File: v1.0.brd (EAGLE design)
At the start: 160 x 100 mm, 44 parts, among them J1 DC-044-A, Q3 6pF@32.7680kHz, U1 MCP23017-E/SO, U10 74HC139N, U2 MCP79412-I/SN, U3 LOPY, U4 GROVE_DC&DC

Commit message: pycom
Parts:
- added X1, X2, X3, X4: JST-XH-05-PIN-ROUND-PAD, Rembrandt Electronics - JST XH Connectors v1-0 2:JST-XH-05-PACKAGE-ROUND-PAD
- added X5: JST-XH-06-PIN-ROUND-PAD, Rembrandt Electronics - JST XH Connectors v1-0 2:JST-XH-06-PACKAGE-ROUND-PAD
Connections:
- removed net LOPY_P0: U3.P$2
- removed net LOPY_P1: U3.P$3
- removed net LOPY_P10: U3.P$12
- removed net LOPY_P11: U3.P$13
- removed net LOPY_P12: U3.P$14
- removed net LOPY_P3: U3.P$5
- removed net LOPY_P4: U3.P$6
- removed net LOPY_P9: U3.P$11
- new net LOPY_CS: X5.6
- new net LOPY_MISO: U3.P$14, X5.4
- new net LOPY_MOSI: U3.P$13, X5.3
- new net LOPY_RX0: U3.P$2, X1.4
- new net LOPY_RX1: U3.P$6, X2.4
- new net LOPY_SCL/CLK: U3.P$12, X3.5, X5.5
- new net LOPY_SDA: U3.P$11, X3.4
- new net LOPY_TX0: U3.P$3, X1.5
- new net LOPY_TX1: U3.P$5, X2.5
- net +5V: now also X1.1, X2.1, X3.1, X5.1
- net GND: now also X1.3, X2.3, X3.3
- net LOPY_3V3: now also X1.2, X2.2, X3.2, X5.2
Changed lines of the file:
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@@
 <attribute name="MPN" value="CC0603KRX7R9BB104" x="-224.79" y="-213.36" size="1.778" layer="27" display="off"/>
 </element>
+<element name="X1" library="Rembrandt Electronics - JST XH Connectors v1-0 2" package="JST-XH-05-PACKAGE-ROUND-PAD" value="JST-XH-05-PIN-ROUND-PAD" x="-213.36" y="-226.06"/>
+<element name="X2" library="Rembrandt Electronics - JST XH Connectors v1-0 2" package="JST-XH-05-PACKAGE-ROUND-PAD" value="JST-XH-05-PIN-ROUND-PAD" x="-213.36" y="-241.3"/>
+<element name="X3" library="Rembrandt Electronics - JST XH Connectors v1-0 2" package="JST-XH-05-PACKAGE-ROUND-PAD" value="JST-XH-05-PIN-ROUND-PAD" x="-213.36" y="-256.54"/>
+<element name="X4" library="Rembrandt Electronics - JST XH Connectors v1-0 2" package="JST-XH-05-PACKAGE-ROUND-PAD" value="JST-XH-05-PIN-ROUND-PAD" x="-213.36" y="-271.78"/>
+<element name="X5" library="Rembrandt Electronics - JST XH Connectors v1-0 2" package="JST-XH-06-PACKAGE-ROUND-PAD" value="JST-XH-06-PIN-ROUND-PAD" x="-212.09" y="-287.02"/>
 </elements>
 <signals>
@@
 <contactref element="C1" pad="2"/>
 <contactref element="C3" pad="2"/>
+<contactref element="X1" pad="3"/>
+<contactref element="X2" pad="3"/>
+<contactref element="X3" pad="3"/>
 <wire x1="-164.719" y1="-102.87" x2="-160.02" y2="-90.678" width="0" layer="19" extent="1-1"/>
 <wire x1="-148.59" y1="-68.58" x2="-160.02" y2="-90.678" width="0" layer="19" extent="1-1"/>
@@
 <wire x1="-219.71" y1="-214.122" x2="-214.63" y2="-185.928" width="0" layer="19" extent="1-1"/>
 <wire x1="-224.79" y1="-214.122" x2="-219.71" y2="-214.122" width="0" layer="19" extent="1-1"/>
+<wire x1="-213.36" y1="-226.06" x2="-219.71" y2="-214.122" width="0" layer="19" extent="1-1"/>
+<wire x1="-213.36" y1="-241.3" x2="-213.36" y2="-226.06" width="0" layer="19" extent="1-1"/>
+<wire x1="-213.36" y1="-256.54" x2="-213.36" y2="-241.3" width="0" layer="19" extent="1-1"/>
 <wire x1="-114.3" y1="4.572" x2="-129.54" y2="-43.688" width="0" layer="19" extent="1-1"/>
 <wire x1="-86.8934" y1="57.5818" x2="-114.3" y2="4.572" width="0" layer="19" extent="1-1"/>
@@
 <contactref element="C13" pad="2"/>
 <contactref element="U3" pad="P$28"/>
+<contactref element="X1" pad="1"/>
+<contactref element="X2" pad="1"/>
+<contactref element="X3" pad="1"/>
+<contactref element="X5" pad="1"/>
+<wire x1="-218.44" y1="-256.54" x2="-218.44" y2="-287.02" width="0" layer="19" extent="1-1"/>
+<wire x1="-218.44" y1="-241.3" x2="-218.44" y2="-256.54" width="0" layer="19" extent="1-1"/>
+<wire x1="-218.44" y1="-226.06" x2="-218.44" y2="-241.3" width="0" layer="19" extent="1-1"/>
+<wire x1="-184.15" y1="-71.12" x2="-218.44" y2="-226.06" width="0" layer="19" extent="1-1"/>
+<wire x1="-140.97" y1="-50.8" x2="-184.15" y2="-71.12" width="0" layer="19" extent="1-1"/>
 <wire x1="-129.54" y1="-45.212" x2="-140.97" y2="-50.8" width="0" layer="19" extent="1-1"/>
 <wire x1="-129.54" y1="-32.512" x2="-129.54" y2="-45.212" width="0" layer="19" extent="1-1"/>
-<wire x1="-184.15" y1="-71.12" x2="-140.97" y2="-50.8" width="0" layer="19" extent="1-1"/>
 <wire x1="-91.9734" y1="57.5818" x2="-129.54" y2="-32.512" width="0" layer="19" extent="1-1"/>
 <wire x1="-89.4334" y1="57.5818" x2="-91.9734" y2="57.5818" width="0" layer="19" extent="1-1"/>
@@
 <signal name="LOPY_3V3">
 <contactref element="U3" pad="P$26"/>
+<contactref element="X1" pad="2"/>
+<contactref element="X2" pad="2"/>
+<contactref element="X3" pad="2"/>
+<contactref element="X5" pad="2"/>
+<wire x1="-215.9" y1="-256.54" x2="-215.9" y2="-287.02" width="0" layer="19" extent="1-1"/>
+<wire x1="-215.9" y1="-241.3" x2="-215.9" y2="-256.54" width="0" layer="19" extent="1-1"/>
+<wire x1="-215.9" y1="-226.06" x2="-215.9" y2="-241.3" width="0" layer="19" extent="1-1"/>
+<wire x1="-184.15" y1="-76.2" x2="-215.9" y2="-226.06" width="0" layer="19" extent="1-1"/>
 </signal>
 <signal name="LOPY_RST">
 <contactref element="U3" pad="P$1"/>
 </signal>
-<signal name="LOPY_P0">
+<signal name="LOPY_RX0">
 <contactref element="U3" pad="P$2"/>
-</signal>
-<signal name="LOPY_P1">
+<contactref element="X1" pad="4"/>
+<wire x1="-201.93" y1="-73.66" x2="-210.82" y2="-226.06" width="0" layer="19" extent="1-1"/>
+</signal>
+<signal name="LOPY_TX0">
 <contactref element="U3" pad="P$3"/>
+<contactref element="X1" pad="5"/>
+<wire x1="-201.93" y1="-76.2" x2="-208.28" y2="-226.06" width="0" layer="19" extent="1-1"/>
 </signal>
 <signal name="LOPY_P2">
 <contactref element="U3" pad="P$4"/>
 </signal>
-<signal name="LOPY_P3">
+<signal name="LOPY_TX1">
 <contactref element="U3" pad="P$5"/>
-</signal>
-<signal name="LOPY_P4">
-<contactref element="U3" pad="P$6"/>
+<contactref element="X2" pad="5"/>
+<wire x1="-201.93" y1="-81.28" x2="-208.28" y2="-241.3" width="0" layer="19" extent="1-1"/>
 </signal>
 <signal name="LOPY_P8">
 <contactref element="U3" pad="P$10"/>
 </signal>
-<signal name="LOPY_P9">
+<signal name="LOPY_SDA">
 <contactref element="U3" pad="P$11"/>
-</signal>
-<signal name="LOPY_P10">
+<contactref element="X3" pad="4"/>
+<wire x1="-201.93" y1="-96.52" x2="-210.82" y2="-256.54" width="0" layer="19" extent="1-1"/>
+</signal>
+<signal name="LOPY_SCL/CLK">
 <contactref element="U3" pad="P$12"/>
-</signal>
-<signal name="LOPY_P11">
+<contactref element="X3" pad="5"/>
+<contactref element="X5" pad="5"/>
+<wire x1="-208.28" y1="-256.54" x2="-208.28" y2="-287.02" width="0" layer="19" extent="1-1"/>
+<wire x1="-201.93" y1="-99.06" x2="-208.28" y2="-256.54" width="0" layer="19" extent="1-1"/>
+</signal>
+<signal name="LOPY_MOSI">
 <contactref element="U3" pad="P$13"/>
-</signal>
-<signal name="LOPY_P12">
+<contactref element="X5" pad="3"/>
+<wire x1="-201.93" y1="-101.6" x2="-213.36" y2="-287.02" width="0" layer="19" extent="1-1"/>
+</signal>
+<signal name="LOPY_MISO">
 <contactref element="U3" pad="P$14"/>
+<contactref element="X5" pad="4"/>
+<wire x1="-201.93" y1="-104.14" x2="-210.82" y2="-287.02" width="0" layer="19" extent="1-1"/>
 </signal>
 <signal name="LOPY_P13">
@@
 <wire x1="-203.0222" y1="-168.275" x2="-212.09" y2="-215.646" width="0" layer="19" extent="1-1"/>
 </signal>
+<signal name="LOPY_RX1">
+<contactref element="X2" pad="4"/>
+<contactref element="U3" pad="P$6"/>
+<wire x1="-201.93" y1="-83.82" x2="-210.82" y2="-241.3" width="0" layer="19" extent="1-1"/>
+</signal>
+<signal name="LOPY_CS">
+<contactref element="X5" pad="6"/>
+</signal>
 </signals>

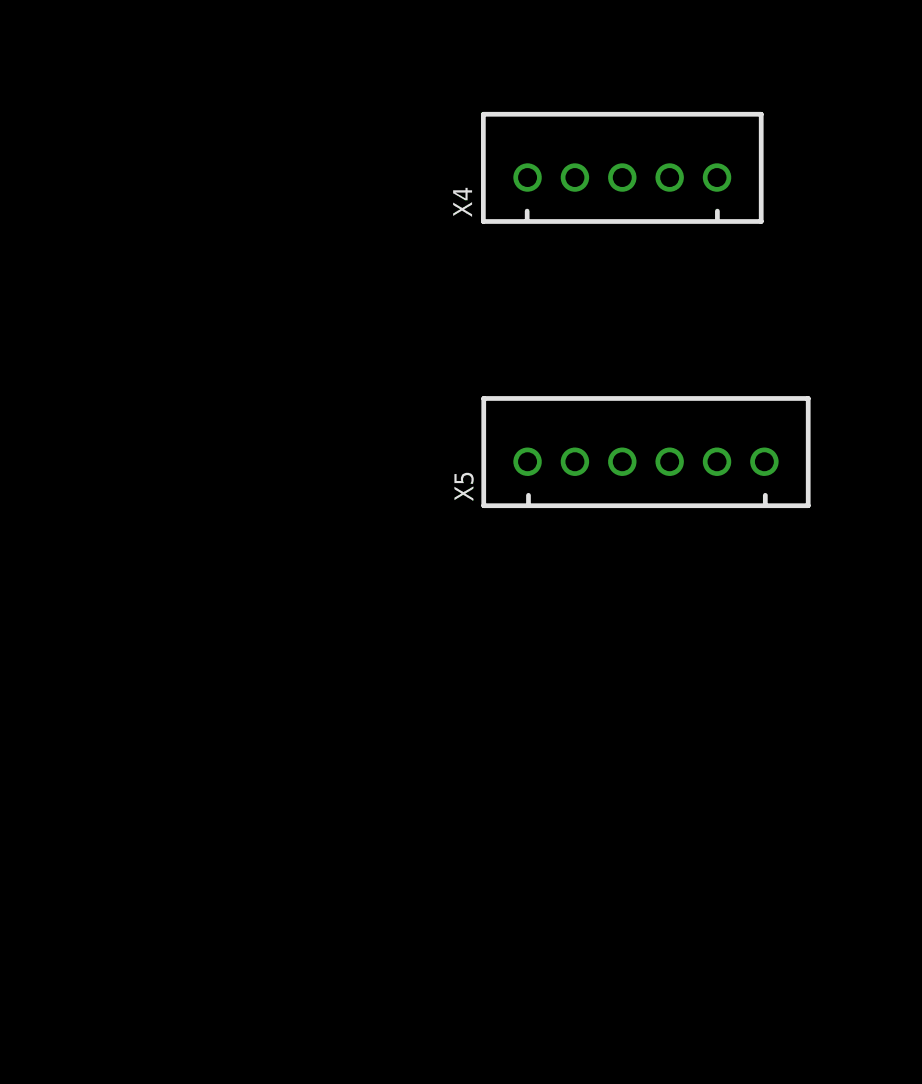
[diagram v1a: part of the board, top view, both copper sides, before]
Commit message: LDO for 5V
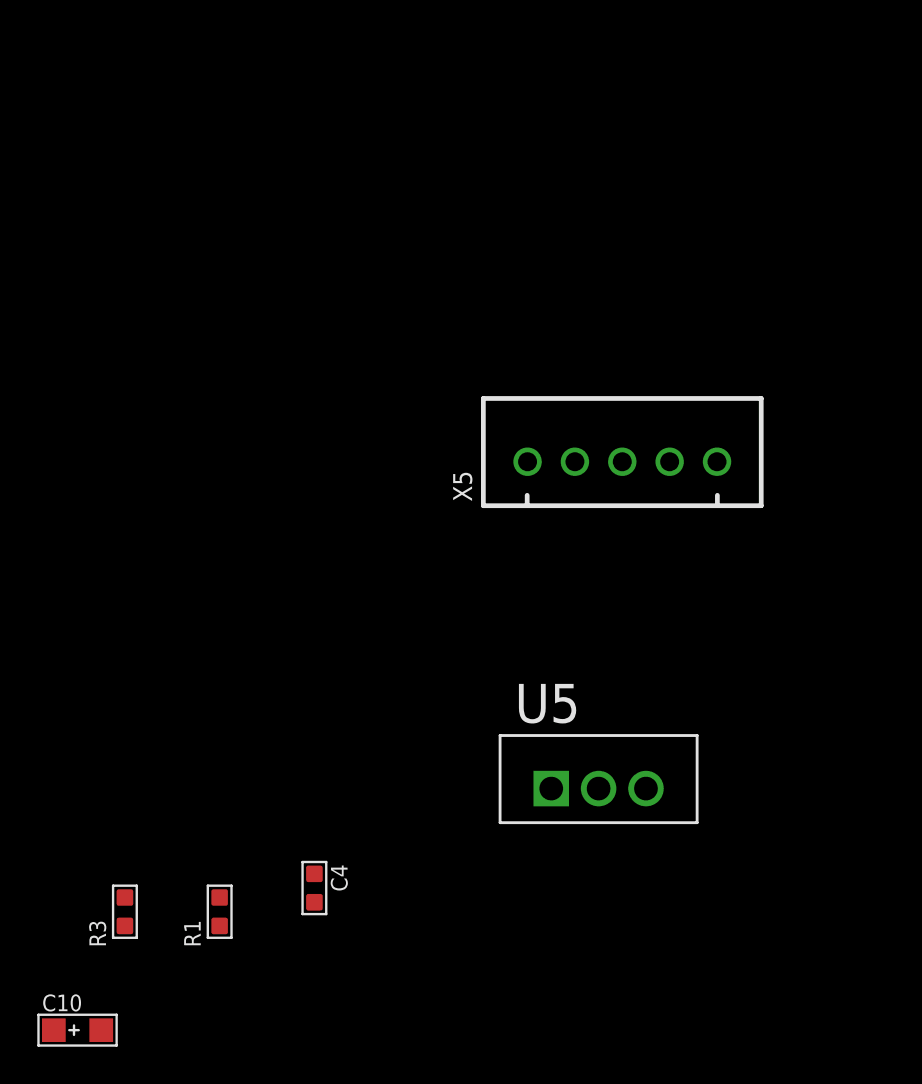
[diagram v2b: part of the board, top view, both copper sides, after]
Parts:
- removed X4: JST-XH-05-PIN-ROUND-PAD, Rembrandt Electronics - JST XH Connectors v1-0 2:JST-XH-05-PACKAGE-ROUND-PAD
- added C10: 10uf, Seeed-Capacitor:AVX-A
- added C4: 10uf, Seeed-Capacitor:C0603
- added R1: 3K, Seeed-Resistor:R0603
- added R3: 1K, Seeed-Resistor:R0603
- added U5: LM1085IT-5.0, imported-parts:TO254P470X1016X2222-3P
- X5: value JST-XH-06-PIN-ROUND-PAD -> JST-XH-05-PIN-ROUND-PAD; device Rembrandt Electronics - JST XH Connectors v1-0 2:JST-XH-06-PACKAGE-ROUND-PAD -> Rembrandt Electronics - JST XH Connectors v1-0 2:JST-XH-05-PACKAGE-ROUND-PAD
- moved X5 1.27 mm to (-213.4, -287.0)
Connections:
- removed net LOPY_CS: X5.6
- new net 6V5: C4.2, TP4.TP, U4.P$5, U4.P$6, U5.3
- new net N$5: R1.2, R3.1, U5.1
- net +5V: now also C10.-, R3.2, U5.2
- net 5V4: no longer TP4.TP, U4.P$5, U4.P$6
- net GND: now also C10.+, C4.1, R1.1
- net LOPY_MISO: now also X5.3; no longer X5.4
- net LOPY_MOSI: now also X5.4; no longer X5.3
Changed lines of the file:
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@@
 <element name="X2" library="Rembrandt Electronics - JST XH Connectors v1-0 2" package="JST-XH-05-PACKAGE-ROUND-PAD" value="JST-XH-05-PIN-ROUND-PAD" x="-213.36" y="-241.3"/>
 <element name="X3" library="Rembrandt Electronics - JST XH Connectors v1-0 2" package="JST-XH-05-PACKAGE-ROUND-PAD" value="JST-XH-05-PIN-ROUND-PAD" x="-213.36" y="-256.54"/>
-<element name="X4" library="Rembrandt Electronics - JST XH Connectors v1-0 2" package="JST-XH-05-PACKAGE-ROUND-PAD" value="JST-XH-05-PIN-ROUND-PAD" x="-213.36" y="-271.78"/>
-<element name="X5" library="Rembrandt Electronics - JST XH Connectors v1-0 2" package="JST-XH-06-PACKAGE-ROUND-PAD" value="JST-XH-06-PIN-ROUND-PAD" x="-212.09" y="-287.02"/>
+<element name="X5" library="Rembrandt Electronics - JST XH Connectors v1-0 2" package="JST-XH-05-PACKAGE-ROUND-PAD" value="JST-XH-05-PIN-ROUND-PAD" x="-213.36" y="-287.02"/>
+<element name="U5" library="imported-parts" package="TO254P470X1016X2222-3P" value="LM1085IT-5.0" x="-212.09" y="-303.53">
+<attribute name="MPN" value="LM1085IT-5.0" x="-212.09" y="-303.53" size="1.778" layer="27" display="off"/>
+<attribute name="OC_FARNELL" value="1469042" x="-212.09" y="-303.53" size="1.778" layer="27" display="off"/>
+<attribute name="OC_NEWARK" value="41K3382" x="-212.09" y="-303.53" size="1.778" layer="27" display="off"/>
+<attribute name="PACKAGE" value="TO-220" x="-212.09" y="-303.53" size="1.778" layer="27" display="off"/>
+<attribute name="SUPPLIER" value="National Semiconductor" x="-212.09" y="-303.53" size="1.778" layer="27" display="off"/>
+</element>
+<element name="C4" library="Seeed-Capacitor" library_urn="urn:adsk.eagle:library:464" package="C0603" value="10uf" x="-229.87" y="-309.88">
+<attribute name="MPN" value="CC0603KRX5R6BB106" x="-229.87" y="-309.88" size="1.778" layer="27" display="off"/>
+</element>
+<element name="R1" library="Seeed-Resistor" library_urn="urn:adsk.eagle:library:474" package="R0603" value="3K" x="-234.95" y="-311.15">
+<attribute name="MPN" value="RC0603FR-073KL" x="-234.95" y="-311.15" size="1.778" layer="27" display="off"/>
+</element>
+<element name="R3" library="Seeed-Resistor" library_urn="urn:adsk.eagle:library:474" package="R0603" value="1K" x="-240.03" y="-311.15">
+<attribute name="MPN" value="RC0603FR-071KL" x="-240.03" y="-311.15" size="1.778" layer="27" display="off"/>
+</element>
+<element name="C10" library="Seeed-Capacitor" library_urn="urn:adsk.eagle:library:464" package="AVX-A" value="10uf" x="-242.57" y="-317.5">
+<attribute name="MPN" value="TAJA106K010RNJ" x="-242.57" y="-317.5" size="1.778" layer="27" display="off"/>
+</element>
 </elements>
 <signals>
@@
 <contactref element="X2" pad="3"/>
 <contactref element="X3" pad="3"/>
+<contactref element="R1" pad="1"/>
+<contactref element="C4" pad="1"/>
+<contactref element="C10" pad="+"/>
 <wire x1="-164.719" y1="-102.87" x2="-160.02" y2="-90.678" width="0" layer="19" extent="1-1"/>
 <wire x1="-148.59" y1="-68.58" x2="-160.02" y2="-90.678" width="0" layer="19" extent="1-1"/>
@@
 <wire x1="-213.36" y1="-256.54" x2="-213.36" y2="-241.3" width="0" layer="19" extent="1-1"/>
 <wire x1="-114.3" y1="4.572" x2="-129.54" y2="-43.688" width="0" layer="19" extent="1-1"/>
+<wire x1="-229.87" y1="-309.118" x2="-213.36" y2="-256.54" width="0" layer="19" extent="1-1"/>
+<wire x1="-234.95" y1="-310.388" x2="-229.87" y2="-309.118" width="0" layer="19" extent="1-1"/>
+<wire x1="-243.84" y1="-317.5" x2="-234.95" y2="-310.388" width="0" layer="19" extent="1-1"/>
 <wire x1="-86.8934" y1="57.5818" x2="-114.3" y2="4.572" width="0" layer="19" extent="1-1"/>
 <wire x1="-81.8134" y1="55.0418" x2="-86.8934" y2="57.5818" width="0" layer="19" extent="1-1"/>
@@
 <contactref element="X3" pad="1"/>
 <contactref element="X5" pad="1"/>
+<contactref element="U5" pad="2"/>
+<contactref element="R3" pad="2"/>
+<contactref element="C10" pad="-"/>
+<wire x1="-214.63" y1="-304.546" x2="-218.44" y2="-287.02" width="0" layer="19" extent="1-1"/>
+<wire x1="-240.03" y1="-311.912" x2="-214.63" y2="-304.546" width="0" layer="19" extent="1-1"/>
+<wire x1="-241.3" y1="-317.5" x2="-240.03" y2="-311.912" width="0" layer="19" extent="1-1"/>
 <wire x1="-218.44" y1="-256.54" x2="-218.44" y2="-287.02" width="0" layer="19" extent="1-1"/>
 <wire x1="-218.44" y1="-241.3" x2="-218.44" y2="-256.54" width="0" layer="19" extent="1-1"/>
@@
 <signal name="LOPY_MOSI">
 <contactref element="U3" pad="P$13"/>
-<contactref element="X5" pad="3"/>
-<wire x1="-201.93" y1="-101.6" x2="-213.36" y2="-287.02" width="0" layer="19" extent="1-1"/>
+<contactref element="X5" pad="4"/>
+<wire x1="-201.93" y1="-101.6" x2="-210.82" y2="-287.02" width="0" layer="19" extent="1-1"/>
 </signal>
 <signal name="LOPY_MISO">
 <contactref element="U3" pad="P$14"/>
-<contactref element="X5" pad="4"/>
-<wire x1="-201.93" y1="-104.14" x2="-210.82" y2="-287.02" width="0" layer="19" extent="1-1"/>
+<contactref element="X5" pad="3"/>
+<wire x1="-201.93" y1="-104.14" x2="-213.36" y2="-287.02" width="0" layer="19" extent="1-1"/>
 </signal>
 <signal name="LOPY_P13">
@@
 </signal>
 <signal name="5V4">
-<contactref element="U4" pad="P$5"/>
-<contactref element="U4" pad="P$6"/>
-<contactref element="TP4" pad="TP"/>
 <contactref element="R7" pad="2"/>
-<wire x1="-176.53" y1="-130.81" x2="-134.62" y2="-32.512" width="0" layer="19" extent="1-1"/>
-<wire x1="-176.53" y1="-133.35" x2="-176.53" y2="-130.81" width="0" layer="19" extent="1-1"/>
-<wire x1="-203.2" y1="-160.02" x2="-176.53" y2="-133.35" width="0" layer="19" extent="1-1"/>
 </signal>
 <signal name="N$3">
@@
 <wire x1="-201.93" y1="-83.82" x2="-210.82" y2="-241.3" width="0" layer="19" extent="1-1"/>
 </signal>
-<signal name="LOPY_CS">
-<contactref element="X5" pad="6"/>
+<signal name="6V5">
+<contactref element="U4" pad="P$5"/>
+<contactref element="U4" pad="P$6"/>
+<contactref element="TP4" pad="TP"/>
+<contactref element="U5" pad="3"/>
+<contactref element="C4" pad="2"/>
+<wire x1="-176.53" y1="-133.35" x2="-203.2" y2="-160.02" width="0" layer="19" extent="1-1"/>
+<wire x1="-176.53" y1="-130.81" x2="-176.53" y2="-133.35" width="0" layer="19" extent="1-1"/>
+<wire x1="-212.09" y1="-304.546" x2="-203.2" y2="-160.02" width="0" layer="19" extent="1-1"/>
+<wire x1="-229.87" y1="-310.642" x2="-212.09" y2="-304.546" width="0" layer="19" extent="1-1"/>
+</signal>
+<signal name="N$5">
+<contactref element="U5" pad="1"/>
+<contactref element="R3" pad="1"/>
+<contactref element="R1" pad="2"/>
+<wire x1="-234.95" y1="-311.912" x2="-240.03" y2="-310.388" width="0" layer="19" extent="1-1"/>
+<wire x1="-217.17" y1="-304.546" x2="-234.95" y2="-311.912" width="0" layer="19" extent="1-1"/>
 </signal>
 </signals>
